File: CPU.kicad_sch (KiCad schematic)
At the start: 14 parts, among them J8 ISP, U4 STM32F405RGTx, Y1 8MHz

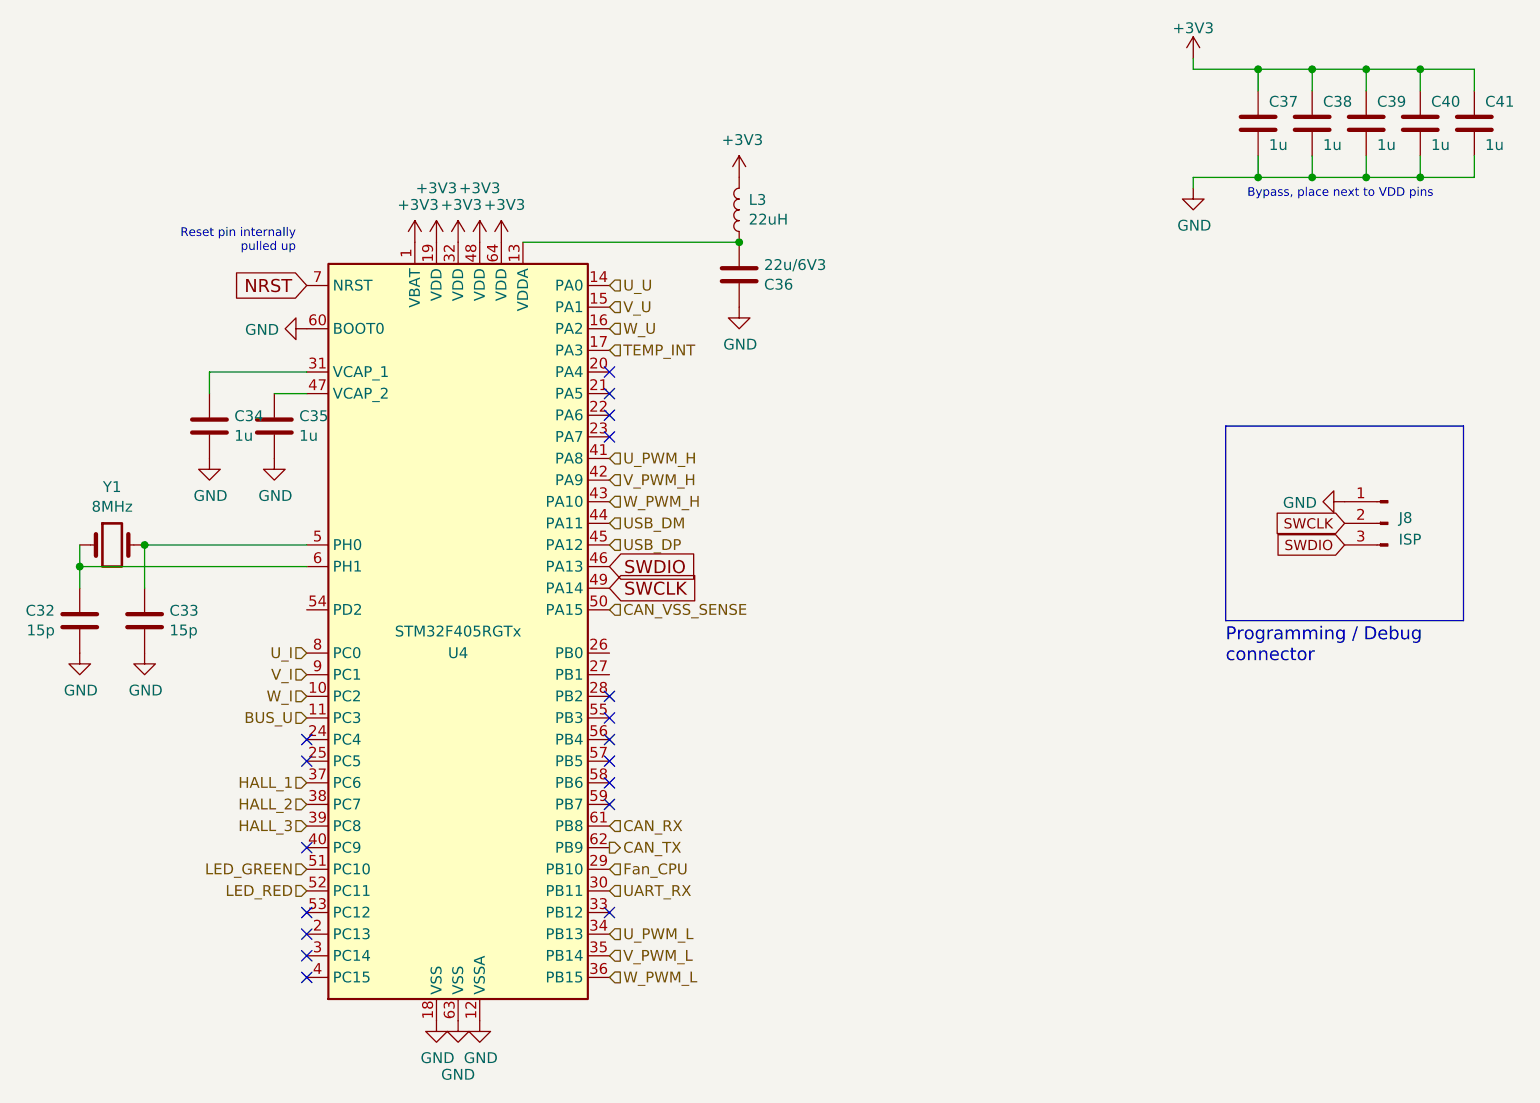
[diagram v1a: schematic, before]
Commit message: HSWR_dual V1: - derived from HSWR V4.1 - STM32F405RG -> IO limited - only 2 phase shunts - no layout work yet
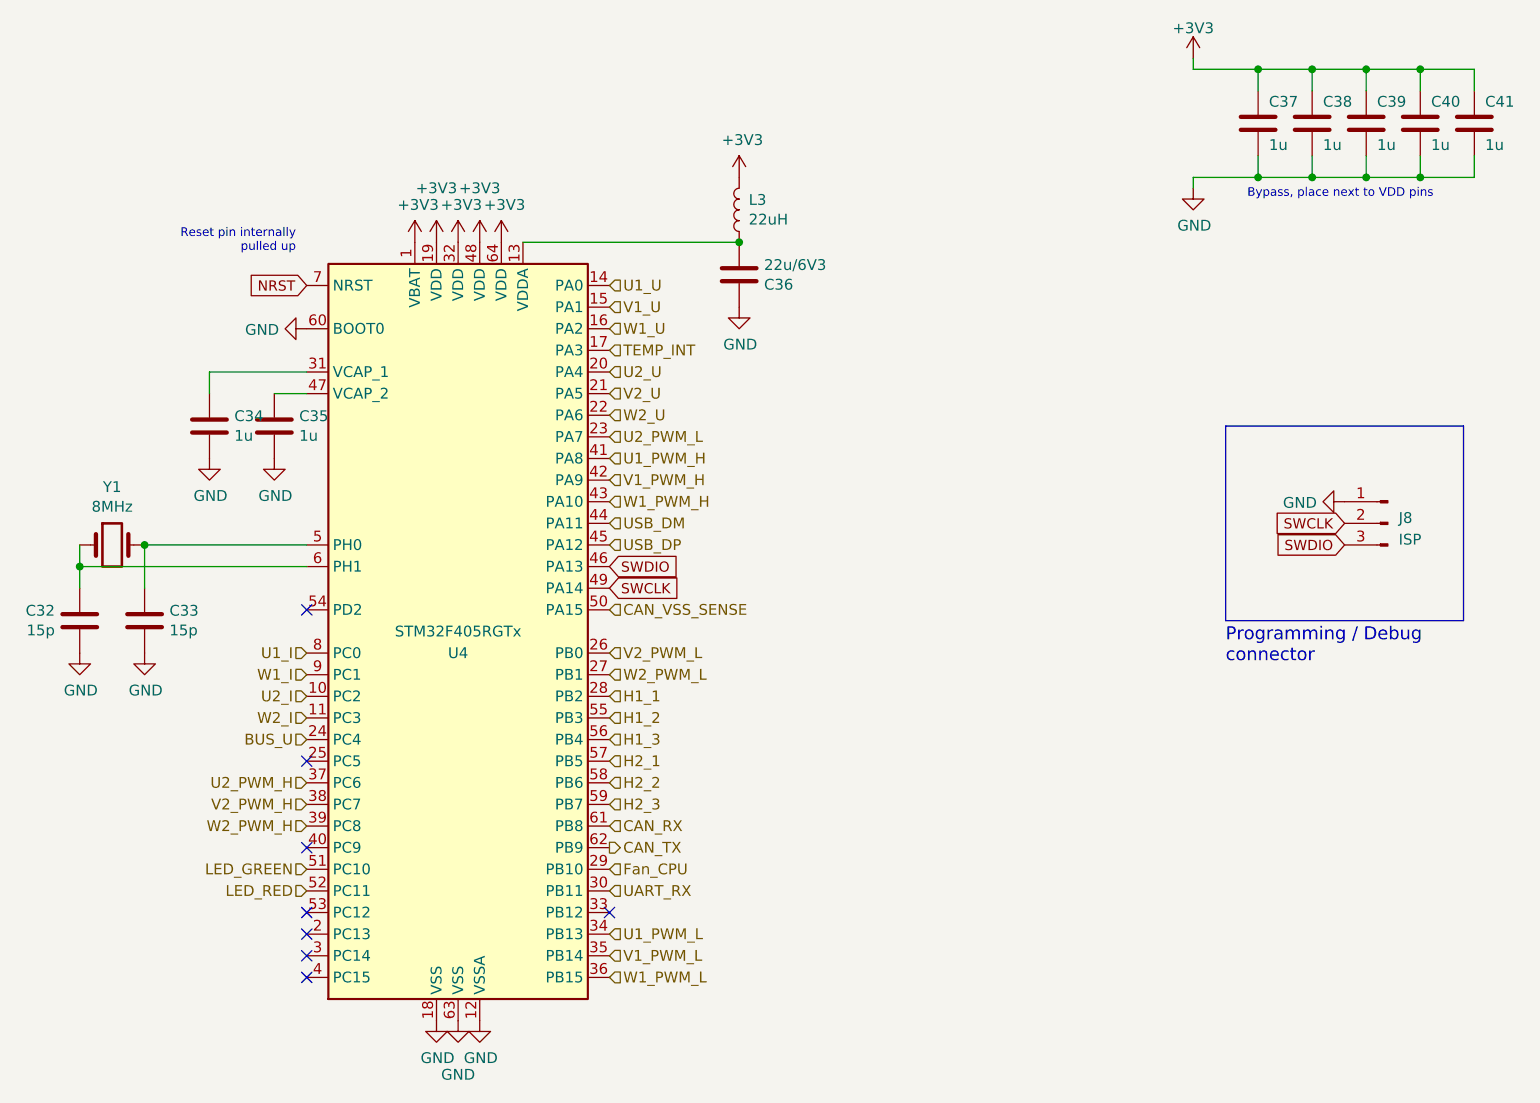
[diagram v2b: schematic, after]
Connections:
- net BUS_U: now also U4.24 (PC4); no longer U4.11 (PC3)
- net U2_U: now reaches U4.20 (PA4)
- net V2_U: now reaches U4.21 (PA5)
- net W2_U: now reaches U4.22 (PA6)
- net U2_PWM_L: now reaches U4.23 (PA7)
- net V2_PWM_L: now reaches U4.26 (PB0)
- net W2_PWM_L: now reaches U4.27 (PB1)
- net H1_1: now reaches U4.28 (PB2)
- net H1_2: now reaches U4.55 (PB3)
- net H1_3: now reaches U4.56 (PB4)
- net H2_1: now reaches U4.57 (PB5)
- net H2_2: now reaches U4.58 (PB6)
- net H2_3: now reaches U4.59 (PB7)
- net HALL_1 renamed U2_PWM_H
- net HALL_2 renamed V2_PWM_H
- net HALL_3 renamed W2_PWM_H
- net U_I renamed U1_I
- net U_PWM_H renamed U1_PWM_H
- net U_PWM_L renamed U1_PWM_L
- net U_U renamed U1_U
- net V_I renamed W1_I
- net V_PWM_H renamed V1_PWM_H
- net V_PWM_L renamed V1_PWM_L
- net V_U renamed V1_U
- net W_I renamed U2_I
- net W_PWM_H renamed W1_PWM_H
- net W_PWM_L renamed W1_PWM_L
- net W_U renamed W1_U
- new net W2_I: U4.11 (PC3)
- no-connect marks 18 -> 8
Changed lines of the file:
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@@
   )
   (no_connect (at 127 106.68))
-  (no_connect (at 162.56 101.6))
   (no_connect (at 127 129.54))
-  (no_connect (at 162.56 66.04))
   (no_connect (at 162.56 124.46))
-  (no_connect (at 162.56 106.68))
-  (no_connect (at 127 104.14))
-  (no_connect (at 162.56 99.06))
-  (no_connect (at 162.56 63.5))
-  (no_connect (at 162.56 68.58))
-  (no_connect (at 162.56 104.14))
+  (no_connect (at 127 88.9))
   (no_connect (at 127 116.84))
-  (no_connect (at 162.56 109.22))
-  (no_connect (at 162.56 60.96))
   (no_connect (at 127 132.08))
   (no_connect (at 127 127))
   (no_connect (at 127 124.46))
-  (no_connect (at 162.56 111.76))
   (wire (pts (xy 127 63.5) (xy 123.19 63.5))
     (stroke (width 0) (type default))
@@
   )
   (global_label "SWDIO" (shape input) (at 162.56 83.82 0)
-    (effects (font (size 1.524 1.524)) (justify left))
+    (effects (font (size 1.2 1.2)) (justify left))
     (property "Intersheetrefs" "${INTERSHEET_REFS}" (at 162.56 83.82 0)
       (effects (font (size 1.27 1.27)) hide)
@@
   )
   (global_label "NRST" (shape input) (at 127 50.8 180)
-    (effects (font (size 1.524 1.524)) (justify right))
+    (effects (font (size 1.2 1.2)) (justify right))
     (property "Intersheetrefs" "${INTERSHEET_REFS}" (at 127 50.8 0)
       (effects (font (size 1.27 1.27)) hide)
@@
   )
   (global_label "SWCLK" (shape input) (at 162.56 86.36 0)
-    (effects (font (size 1.524 1.524)) (justify left))
+    (effects (font (size 1.2 1.2)) (justify left))
     (property "Intersheetrefs" "${INTERSHEET_REFS}" (at 162.56 86.36 0)
       (effects (font (size 1.27 1.27)) hide)
@@
     )
   )
-  (hierarchical_label "HALL_2" (shape input) (at 127 111.76 180) (fields_autoplaced)
+  (hierarchical_label "H1_2" (shape input) (at 162.56 101.6 0) (fields_autoplaced)
+    (effects (font (size 1.27 1.27)) (justify left))
+  )
+  (hierarchical_label "V1_PWM_L" (shape input) (at 162.56 129.54 0) (fields_autoplaced)
+    (effects (font (size 1.27 1.27)) (justify left))
+  )
+  (hierarchical_label "V1_PWM_H" (shape input) (at 162.56 73.66 0) (fields_autoplaced)
+    (effects (font (size 1.27 1.27)) (justify left))
+  )
+  (hierarchical_label "H2_1" (shape input) (at 162.56 106.68 0) (fields_autoplaced)
+    (effects (font (size 1.27 1.27)) (justify left))
+  )
+  (hierarchical_label "W1_I" (shape input) (at 127 96.52 180) (fields_autoplaced)
     (effects (font (size 1.27 1.27)) (justify right))
   )
-  (hierarchical_label "V_PWM_L" (shape input) (at 162.56 129.54 0) (fields_autoplaced)
-    (effects (font (size 1.27 1.27)) (justify left))
-  )
-  (hierarchical_label "V_PWM_H" (shape input) (at 162.56 73.66 0) (fields_autoplaced)
-    (effects (font (size 1.27 1.27)) (justify left))
-  )
-  (hierarchical_label "V_I" (shape input) (at 127 96.52 180) (fields_autoplaced)
+  (hierarchical_label "CAN_RX" (shape input) (at 162.56 114.3 0) (fields_autoplaced)
+    (effects (font (size 1.27 1.27)) (justify left))
+  )
+  (hierarchical_label "V2_U" (shape input) (at 162.56 63.5 0) (fields_autoplaced)
+    (effects (font (size 1.27 1.27)) (justify left))
+  )
+  (hierarchical_label "U2_PWM_L" (shape input) (at 162.56 68.58 0) (fields_autoplaced)
+    (effects (font (size 1.27 1.27)) (justify left))
+  )
+  (hierarchical_label "U2_PWM_H" (shape input) (at 127 109.22 180) (fields_autoplaced)
     (effects (font (size 1.27 1.27)) (justify right))
   )
-  (hierarchical_label "CAN_RX" (shape input) (at 162.56 114.3 0) (fields_autoplaced)
-    (effects (font (size 1.27 1.27)) (justify left))
-  )
-  (hierarchical_label "W_I" (shape input) (at 127 99.06 180) (fields_autoplaced)
+  (hierarchical_label "W2_PWM_H" (shape input) (at 127 114.3 180) (fields_autoplaced)
     (effects (font (size 1.27 1.27)) (justify right))
   )
+  (hierarchical_label "V2_PWM_H" (shape input) (at 127 111.76 180) (fields_autoplaced)
+    (effects (font (size 1.27 1.27)) (justify right))
+  )
+  (hierarchical_label "H2_3" (shape input) (at 162.56 111.76 0) (fields_autoplaced)
+    (effects (font (size 1.27 1.27)) (justify left))
+  )
   (hierarchical_label "UART_RX" (shape input) (at 162.56 121.92 0) (fields_autoplaced)
     (effects (font (size 1.27 1.27)) (justify left))
@@
     (effects (font (size 1.27 1.27)) (justify left))
   )
-  (hierarchical_label "HALL_1" (shape input) (at 127 109.22 180) (fields_autoplaced)
-    (effects (font (size 1.27 1.27)) (justify right))
+  (hierarchical_label "H1_1" (shape input) (at 162.56 99.06 0) (fields_autoplaced)
+    (effects (font (size 1.27 1.27)) (justify left))
   )
   (hierarchical_label "LED_RED" (shape input) (at 127 121.92 180) (fields_autoplaced)
@@
     (effects (font (size 1.27 1.27)) (justify right))
   )
-  (hierarchical_label "W_U" (shape input) (at 162.56 55.88 0) (fields_autoplaced)
+  (hierarchical_label "W1_U" (shape input) (at 162.56 55.88 0) (fields_autoplaced)
+    (effects (font (size 1.27 1.27)) (justify left))
+  )
+  (hierarchical_label "H2_2" (shape input) (at 162.56 109.22 0) (fields_autoplaced)
     (effects (font (size 1.27 1.27)) (justify left))
   )
@@
     (effects (font (size 1.27 1.27)) (justify left))
   )
-  (hierarchical_label "W_PWM_L" (shape input) (at 162.56 132.08 0) (fields_autoplaced)
-    (effects (font (size 1.27 1.27)) (justify left))
-  )
-  (hierarchical_label "HALL_3" (shape input) (at 127 114.3 180) (fields_autoplaced)
+  (hierarchical_label "W1_PWM_L" (shape input) (at 162.56 132.08 0) (fields_autoplaced)
+    (effects (font (size 1.27 1.27)) (justify left))
+  )
+  (hierarchical_label "H1_3" (shape input) (at 162.56 104.14 0) (fields_autoplaced)
+    (effects (font (size 1.27 1.27)) (justify left))
+  )
+  (hierarchical_label "V1_U" (shape input) (at 162.56 53.34 0) (fields_autoplaced)
+    (effects (font (size 1.27 1.27)) (justify left))
+  )
+  (hierarchical_label "U1_U" (shape input) (at 162.56 50.8 0) (fields_autoplaced)
+    (effects (font (size 1.27 1.27)) (justify left))
+  )
+  (hierarchical_label "USB_DM" (shape input) (at 162.56 78.74 0) (fields_autoplaced)
+    (effects (font (size 1.27 1.27)) (justify left))
+  )
+  (hierarchical_label "W2_PWM_L" (shape input) (at 162.56 96.52 0) (fields_autoplaced)
+    (effects (font (size 1.27 1.27)) (justify left))
+  )
+  (hierarchical_label "U1_PWM_L" (shape input) (at 162.56 127 0) (fields_autoplaced)
+    (effects (font (size 1.27 1.27)) (justify left))
+  )
+  (hierarchical_label "Fan_CPU" (shape input) (at 162.56 119.38 0) (fields_autoplaced)
+    (effects (font (size 1.27 1.27)) (justify left))
+  )
+  (hierarchical_label "W2_U" (shape input) (at 162.56 66.04 0) (fields_autoplaced)
+    (effects (font (size 1.27 1.27)) (justify left))
+  )
+  (hierarchical_label "BUS_U" (shape input) (at 127 104.14 180) (fields_autoplaced)
     (effects (font (size 1.27 1.27)) (justify right))
   )
-  (hierarchical_label "V_U" (shape input) (at 162.56 53.34 0) (fields_autoplaced)
-    (effects (font (size 1.27 1.27)) (justify left))
-  )
-  (hierarchical_label "U_U" (shape input) (at 162.56 50.8 0) (fields_autoplaced)
-    (effects (font (size 1.27 1.27)) (justify left))
-  )
-  (hierarchical_label "USB_DM" (shape input) (at 162.56 78.74 0) (fields_autoplaced)
-    (effects (font (size 1.27 1.27)) (justify left))
-  )
-  (hierarchical_label "U_PWM_L" (shape input) (at 162.56 127 0) (fields_autoplaced)
-    (effects (font (size 1.27 1.27)) (justify left))
-  )
-  (hierarchical_label "Fan_CPU" (shape input) (at 162.56 119.38 0) (fields_autoplaced)
-    (effects (font (size 1.27 1.27)) (justify left))
-  )
-  (hierarchical_label "BUS_U" (shape input) (at 127 101.6 180) (fields_autoplaced)
+  (hierarchical_label "W1_PWM_H" (shape input) (at 162.56 76.2 0) (fields_autoplaced)
+    (effects (font (size 1.27 1.27)) (justify left))
+  )
+  (hierarchical_label "U2_I" (shape input) (at 127 99.06 180) (fields_autoplaced)
     (effects (font (size 1.27 1.27)) (justify right))
   )
-  (hierarchical_label "W_PWM_H" (shape input) (at 162.56 76.2 0) (fields_autoplaced)
-    (effects (font (size 1.27 1.27)) (justify left))
-  )
-  (hierarchical_label "U_I" (shape input) (at 127 93.98 180) (fields_autoplaced)
+  (hierarchical_label "V2_PWM_L" (shape input) (at 162.56 93.98 0) (fields_autoplaced)
+    (effects (font (size 1.27 1.27)) (justify left))
+  )
+  (hierarchical_label "W2_I" (shape input) (at 127 101.6 180) (fields_autoplaced)
     (effects (font (size 1.27 1.27)) (justify right))
   )
+  (hierarchical_label "U1_I" (shape input) (at 127 93.98 180) (fields_autoplaced)
+    (effects (font (size 1.27 1.27)) (justify right))
+  )
   (hierarchical_label "TEMP_INT" (shape input) (at 162.56 58.42 0) (fields_autoplaced)
     (effects (font (size 1.27 1.27)) (justify left))
   )
-  (hierarchical_label "U_PWM_H" (shape input) (at 162.56 71.12 0) (fields_autoplaced)
+  (hierarchical_label "U1_PWM_H" (shape input) (at 162.56 71.12 0) (fields_autoplaced)
     (effects (font (size 1.27 1.27)) (justify left))
   )
@@
     (effects (font (size 1.27 1.27)) (justify left))
   )
+  (hierarchical_label "U2_U" (shape input) (at 162.56 60.96 0) (fields_autoplaced)
+    (effects (font (size 1.27 1.27)) (justify left))
+  )

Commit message: - some work on schematic
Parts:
- renumbered C32 to C16, C33 to C17, C34 to C18, C35 to C19, C36 to C20, C37 to C21, C38 to C22, C39 to C23, C40 to C24, C41 to C25, J8 to J12, L3 to L1, U4 to U8

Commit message: - layout almost finished
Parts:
- removed C23: 1u, Capacitor_SMD:C_0805_2012Metric, symbol Device:C
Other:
- moved on the sheet: C24, C25
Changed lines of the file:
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@@
   (junction (at 245.11 25.4) (diameter 0) (color 0 0 0 0)
   )
-  (junction (at 251.46 38.1) (diameter 0) (color 0 0 0 0)
-  )
   (junction (at 238.76 38.1) (diameter 0) (color 0 0 0 0)
   )
@@
   (junction (at 251.46 25.4) (diameter 0) (color 0 0 0 0)
   )
-  (junction (at 257.81 25.4) (diameter 0) (color 0 0 0 0)
-  )
   (junction (at 238.76 25.4) (diameter 0) (color 0 0 0 0)
   )
@@
   (junction (at 245.11 38.1) (diameter 0) (color 0 0 0 0)
   )
-  (junction (at 257.81 38.1) (diameter 0) (color 0 0 0 0)
+  (junction (at 251.46 38.1) (diameter 0) (color 0 0 0 0)
   )
   (junction (at 107.95 81.28) (diameter 0) (color 0 0 0 0)
@@
     (stroke (width 0) (type default))
   )
-  (wire (pts (xy 257.81 25.4) (xy 257.81 27.94))
+  (wire (pts (xy 251.46 25.4) (xy 251.46 27.94))
     (stroke (width 0) (type default))
   )
@@
     (stroke (width 0) (type default))
   )
-  (wire (pts (xy 264.16 38.1) (xy 264.16 35.56))
+  (wire (pts (xy 257.81 38.1) (xy 257.81 35.56))
     (stroke (width 0) (type default))
   )
@@
     (stroke (width 0) (type default))
   )
-  (wire (pts (xy 251.46 38.1) (xy 251.46 35.56))
-    (stroke (width 0) (type default))
-  )
   (polyline (pts (xy 234.95 90.17) (xy 262.89 90.17))
     (stroke (width 0) (type default))
@@
     (stroke (width 0) (type default))
   )
-  (wire (pts (xy 257.81 38.1) (xy 257.81 35.56))
+  (wire (pts (xy 251.46 38.1) (xy 251.46 35.56))
     (stroke (width 0) (type default))
   )
-  (wire (pts (xy 251.46 38.1) (xy 257.81 38.1))
+  (wire (pts (xy 245.11 38.1) (xy 251.46 38.1))
     (stroke (width 0) (type default))
   )
@@
     (stroke (width 0) (type default))
   )
-  (wire (pts (xy 264.16 25.4) (xy 264.16 27.94))
+  (wire (pts (xy 257.81 25.4) (xy 257.81 27.94))
     (stroke (width 0) (type default))
   )
@@
     (stroke (width 0) (type default))
   )
-  (wire (pts (xy 251.46 25.4) (xy 257.81 25.4))
-    (stroke (width 0) (type default))
-  )
   (wire (pts (xy 152.4 45.72) (xy 177.8 45.72))
     (stroke (width 0) (type default))
@@
     (stroke (width 0) (type default))
   )
-  (wire (pts (xy 257.81 25.4) (xy 264.16 25.4))
-    (stroke (width 0) (type default))
-  )
-  (wire (pts (xy 245.11 38.1) (xy 251.46 38.1))
-    (stroke (width 0) (type default))
-  )
-  (wire (pts (xy 251.46 25.4) (xy 251.46 27.94))
+  (wire (pts (xy 251.46 25.4) (xy 257.81 25.4))
     (stroke (width 0) (type default))
   )
-  (wire (pts (xy 257.81 38.1) (xy 264.16 38.1))
+  (wire (pts (xy 251.46 38.1) (xy 257.81 38.1))
     (stroke (width 0) (type default))
   )
@@
   (symbol (lib_id "Device:C") (at 251.46 31.75 0) (unit 1)
     (in_bom yes) (on_board yes) (dnp no)
-    (property "Reference" "C23" (at 252.73 29.21 0)
+    (property "Reference" "C24" (at 252.73 29.21 0)
       (effects (font (size 1.27 1.27)) (justify left))
     )
@@
       (project "HSWR"
         (path "/51094070-255e-40e7-bed5-d199e288e5dd/00000000-0000-0000-0000-00005899e230"
-          (reference "C23") (unit 1)
+          (reference "C24") (unit 1)
         )
       )
@@
   (symbol (lib_id "Device:C") (at 257.81 31.75 0) (unit 1)
     (in_bom yes) (on_board yes) (dnp no)
-    (property "Reference" "C24" (at 259.08 29.21 0)
+    (property "Reference" "C25" (at 259.08 29.21 0)
       (effects (font (size 1.27 1.27)) (justify left))
     )
@@
       (effects (font (size 1.27 1.27)) hide)
     )
-    (pin "1")
-    (pin "2")
-    (instances
-      (project "HSWR"
-        (path "/51094070-255e-40e7-bed5-d199e288e5dd/00000000-0000-0000-0000-00005899e230"
-          (reference "C24") (unit 1)
-        )
-      )
-    )
-  )
-  (symbol (lib_id "Device:C") (at 264.16 31.75 0) (unit 1)
-    (in_bom yes) (on_board yes) (dnp no)
-    (property "Reference" "C25" (at 265.43 29.21 0)
-      (effects (font (size 1.27 1.27)) (justify left))
-    )
-    (property "Value" "1u" (at 265.43 34.29 0)
-      (effects (font (size 1.27 1.27)) (justify left))
-    )
-    (property "Footprint" "Capacitor_SMD:C_0805_2012Metric" (at 265.1252 35.56 0)
-      (effects (font (size 1.27 1.27)) hide)
-    )
-    (property "Datasheet" "~" (at 264.16 31.75 0)
-      (effects (font (size 1.27 1.27)) hide)
-    )
